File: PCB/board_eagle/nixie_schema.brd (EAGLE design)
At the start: 150 x 170 mm, 102 parts, among them P1 100k, Q1 BC856B, Q2 IRF740S, U2 MC7940N

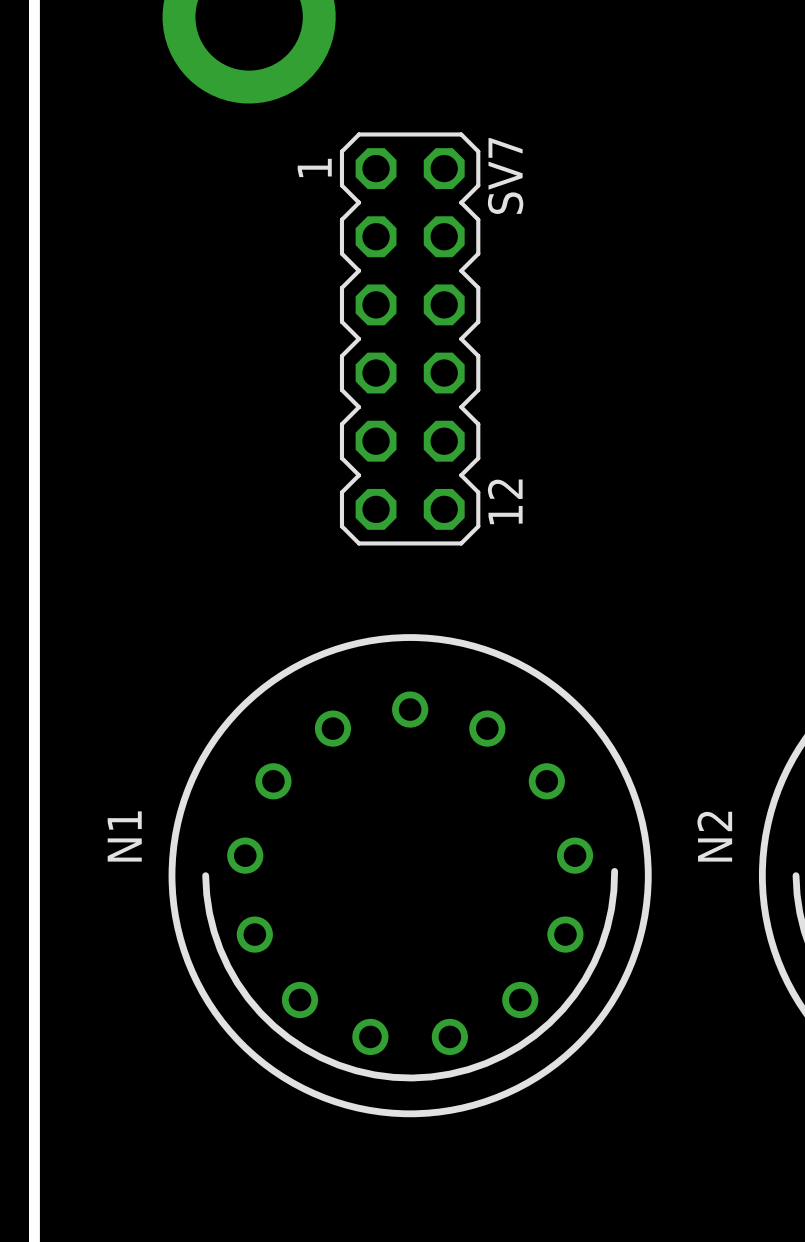
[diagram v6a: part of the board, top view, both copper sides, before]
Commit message: Top board first route
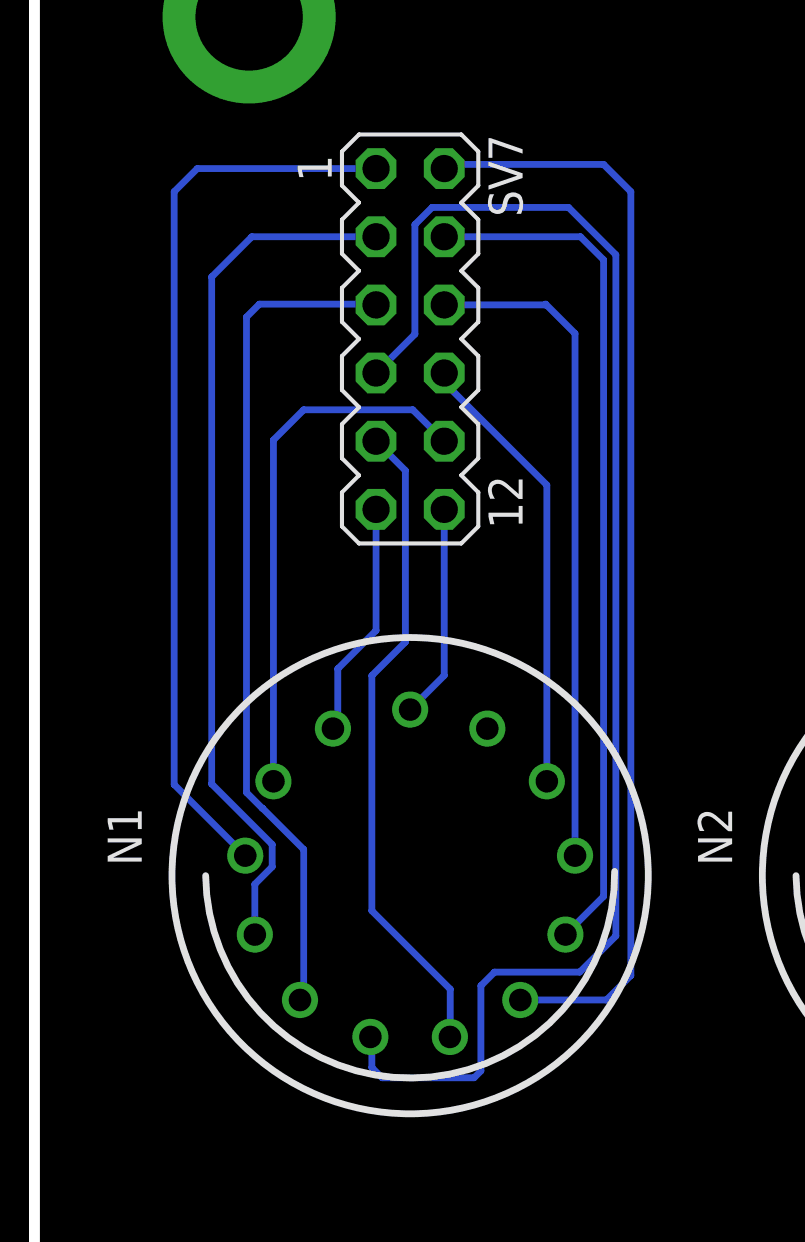
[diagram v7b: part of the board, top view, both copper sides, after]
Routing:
- net N$30: track 0.00 -> 54.5 mm
- net N$28: track 0.00 -> 41.1 mm
- net N$33: track 0.00 -> 33.7 mm
- net N$32: track 0.00 -> 32.5 mm
- net N$27: track 0.00 -> 32.0 mm
- net N$31: track 0.00 -> 31.4 mm
- net N$26: track 0.00 -> 24.8 mm
- net N$29: track 0.00 -> 24.4 mm
- net N$24: track 0.00 -> 20.0 mm
- net N$25: track 0.00 -> 16.8 mm
- net N$94: track 0.00 -> 8.83 mm
- net N$10: track 0.00 -> 7.99 mm
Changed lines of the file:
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@@
 <contactref element="SV7" pad="10"/>
 <contactref element="N1" pad="0"/>
-<wire x1="15.27" y1="-33.81" x2="8.9058" y2="-46.4837" width="0" layer="19" extent="1-1"/>
+<wire x1="8.9058" y1="-33.7662" x2="10.033" y2="-32.639" width="0.254" layer="16"/>
+<wire x1="10.033" y1="-32.639" x2="14.099" y2="-32.639" width="0.254" layer="16"/>
+<wire x1="14.099" y1="-32.639" x2="15.27" y2="-33.81" width="0.254" layer="16"/>
+<wire x1="8.9058" y1="-46.4837" x2="8.9058" y2="-33.7662" width="0.254" layer="16"/>
 </signal>
 <signal name="N$25">
 <contactref element="SV7" pad="8"/>
 <contactref element="N1" pad="1"/>
-<wire x1="15.27" y1="-31.27" x2="19.0942" y2="-46.4837" width="0" layer="19" extent="1-1"/>
+<wire x1="15.27" y1="-31.6188125" x2="15.27" y2="-31.27" width="0.254" layer="16"/>
+<wire x1="19.0942" y1="-46.4837" x2="19.0942" y2="-35.4430125" width="0.254" layer="16"/>
+<wire x1="19.0942" y1="-35.4430125" x2="15.27" y2="-31.6188125" width="0.254" layer="16"/>
 </signal>
 <signal name="N$26">
 <contactref element="SV7" pad="6"/>
 <contactref element="N1" pad="2"/>
-<wire x1="15.27" y1="-28.73" x2="20.1448" y2="-49.2539" width="0" layer="19" extent="1-1"/>
+<wire x1="20.1448" y1="-49.2539" x2="20.1448" y2="-29.7968" width="0.254" layer="16"/>
+<wire x1="19.05" y1="-28.702" x2="20.1448" y2="-29.7968" width="0.254" layer="16"/>
+<wire x1="15.27" y1="-28.73" x2="19.022" y2="-28.73" width="0.254" layer="16"/>
+<wire x1="19.022" y1="-28.73" x2="19.05" y2="-28.702" width="0.254" layer="16"/>
 </signal>
 <signal name="N$27">
 <contactref element="SV7" pad="4"/>
 <contactref element="N1" pad="3"/>
-<wire x1="15.27" y1="-26.19" x2="19.7877" y2="-52.195" width="0" layer="19" extent="1-1"/>
+<wire x1="15.27" y1="-26.19" x2="20.348" y2="-26.19" width="0.254" layer="16"/>
+<wire x1="20.348" y1="-26.19" x2="21.209" y2="-27.051" width="0.254" layer="16"/>
+<wire x1="21.209" y1="-27.051" x2="21.209" y2="-50.7737" width="0.254" layer="16"/>
+<wire x1="21.209" y1="-50.7737" x2="19.7877" y2="-52.195" width="0.254" layer="16"/>
 </signal>
 <signal name="N$28">
 <contactref element="SV7" pad="2"/>
 <contactref element="N1" pad="4"/>
-<wire x1="15.27" y1="-23.65" x2="18.1047" y2="-54.6332" width="0" layer="19" extent="1-1"/>
+<wire x1="18.1047" y1="-54.6332" x2="21.3128" y2="-54.6332" width="0.254" layer="16"/>
+<wire x1="21.3128" y1="-54.6332" x2="22.225" y2="-53.721" width="0.254" layer="16"/>
+<wire x1="22.225" y1="-53.721" x2="22.225" y2="-24.511" width="0.254" layer="16"/>
+<wire x1="22.225" y1="-24.511" x2="21.209" y2="-23.495" width="0.254" layer="16"/>
+<wire x1="21.209" y1="-23.495" x2="15.425" y2="-23.495" width="0.254" layer="16"/>
+<wire x1="15.425" y1="-23.495" x2="15.27" y2="-23.65" width="0.254" layer="16"/>
 </signal>
 <signal name="N$29">
 <contactref element="SV7" pad="9"/>
 <contactref element="N1" pad="5"/>
-<wire x1="12.73" y1="-33.81" x2="15.4813" y2="-56.0101" width="0" layer="19" extent="1-1"/>
+<wire x1="12.73" y1="-33.81" x2="13.8222" y2="-34.9022" width="0.254" layer="16"/>
+<wire x1="13.8222" y1="-41.2958" x2="12.573" y2="-42.545" width="0.254" layer="16"/>
+<wire x1="12.573" y1="-42.545" x2="12.573" y2="-51.308" width="0.254" layer="16"/>
+<wire x1="12.573" y1="-51.308" x2="15.494" y2="-54.229" width="0.254" layer="16"/>
+<wire x1="15.494" y1="-54.229" x2="15.494" y2="-55.9974" width="0.254" layer="16"/>
+<wire x1="15.494" y1="-55.9974" x2="15.4813" y2="-56.0101" width="0.254" layer="16"/>
+<wire x1="13.8222" y1="-34.9022" x2="13.8222" y2="-41.2958" width="0.254" layer="16"/>
 </signal>
 <signal name="N$30">
 <contactref element="SV7" pad="7"/>
 <contactref element="N1" pad="6"/>
-<wire x1="12.73" y1="-31.27" x2="12.5187" y2="-56.0101" width="0" layer="19" extent="1-1"/>
+<wire x1="14.81759375" y1="-25.0978" x2="14.1778" y2="-25.73759375" width="0.254" layer="16"/>
+<wire x1="19.90238125" y1="-25.0978" x2="21.6662" y2="-26.86161875" width="0.254" layer="16"/>
+<wire x1="19.90238125" y1="-25.0978" x2="14.81759375" y2="-25.0978" width="0.254" layer="16"/>
+<wire x1="14.1778" y1="-29.8222" x2="12.73" y2="-31.27" width="0.254" layer="16"/>
+<wire x1="14.1778" y1="-25.73759375" x2="14.1778" y2="-29.8222" width="0.254" layer="16"/>
+<wire x1="21.6662" y1="-52.2478" x2="20.32" y2="-53.594" width="0.254" layer="16"/>
+<wire x1="20.32" y1="-53.594" x2="17.145" y2="-53.594" width="0.254" layer="16"/>
+<wire x1="17.145" y1="-53.594" x2="16.637" y2="-54.102" width="0.254" layer="16"/>
+<wire x1="16.637" y1="-54.102" x2="16.637" y2="-57.277" width="0.254" layer="16"/>
+<wire x1="16.637" y1="-57.277" x2="16.383" y2="-57.531" width="0.254" layer="16"/>
+<wire x1="16.383" y1="-57.531" x2="12.954" y2="-57.531" width="0.254" layer="16"/>
+<wire x1="12.954" y1="-57.531" x2="12.573" y2="-57.15" width="0.254" layer="16"/>
+<wire x1="12.573" y1="-57.15" x2="12.573" y2="-56.0644" width="0.254" layer="16"/>
+<wire x1="12.573" y1="-56.0644" x2="12.5187" y2="-56.0101" width="0.254" layer="16"/>
+<wire x1="21.6662" y1="-26.86161875" x2="21.6662" y2="-52.2478" width="0.254" layer="16"/>
 </signal>
 <signal name="N$31">
 <contactref element="SV7" pad="5"/>
 <contactref element="N1" pad="7"/>
-<wire x1="12.73" y1="-28.73" x2="9.8953" y2="-54.6332" width="0" layer="19" extent="1-1"/>
+<wire x1="8.48984375" y1="-47.4879" x2="8.4989" y2="-47.4879" width="0.254" layer="16"/>
+<wire x1="8.4989" y1="-47.4879" x2="10.033" y2="-49.022" width="0.254" layer="16"/>
+<wire x1="10.033" y1="-49.022" x2="10.033" y2="-54.4955" width="0.254" layer="16"/>
+<wire x1="10.033" y1="-54.4955" x2="9.8953" y2="-54.6332" width="0.254" layer="16"/>
+<wire x1="8.48984375" y1="-47.4879" x2="7.9016" y2="-46.89965625" width="0.254" layer="16"/>
+<wire x1="7.9016" y1="-29.1824" x2="8.382" y2="-28.702" width="0.254" layer="16"/>
+<wire x1="8.382" y1="-28.702" x2="12.702" y2="-28.702" width="0.254" layer="16"/>
+<wire x1="12.702" y1="-28.702" x2="12.73" y2="-28.73" width="0.254" layer="16"/>
+<wire x1="7.9016" y1="-46.89965625" x2="7.9016" y2="-29.1824" width="0.254" layer="16"/>
 </signal>
 <signal name="N$32">
 <contactref element="SV7" pad="3"/>
 <contactref element="N1" pad="8"/>
-<wire x1="12.73" y1="-26.19" x2="8.2123" y2="-52.195" width="0" layer="19" extent="1-1"/>
+<wire x1="12.73" y1="-26.19" x2="8.1" y2="-26.19" width="0.254" layer="16"/>
+<wire x1="8.1" y1="-26.19" x2="6.604" y2="-27.686" width="0.254" layer="16"/>
+<wire x1="8.8594" y1="-48.83794375" x2="8.8594" y2="-49.66985625" width="0.254" layer="16"/>
+<wire x1="6.604" y1="-27.686" x2="6.604" y2="-46.58254375" width="0.254" layer="16"/>
+<wire x1="6.604" y1="-46.58254375" x2="8.8594" y2="-48.83794375" width="0.254" layer="16"/>
+<wire x1="8.8594" y1="-49.66985625" x2="8.2123" y2="-50.31695625" width="0.254" layer="16"/>
+<wire x1="8.2123" y1="-50.31695625" x2="8.2123" y2="-52.195" width="0.254" layer="16"/>
 </signal>
 <signal name="N$33">
 <contactref element="SV7" pad="1"/>
 <contactref element="N1" pad="9"/>
-<wire x1="12.73" y1="-23.65" x2="7.8552" y2="-49.2539" width="0" layer="19" extent="1-1"/>
+<wire x1="12.73" y1="-23.65" x2="6.068" y2="-23.65" width="0.254" layer="16"/>
+<wire x1="6.068" y1="-23.65" x2="5.207" y2="-24.511" width="0.254" layer="16"/>
+<wire x1="5.207" y1="-24.511" x2="5.207" y2="-46.6057" width="0.254" layer="16"/>
+<wire x1="5.207" y1="-46.6057" x2="7.8552" y2="-49.2539" width="0.254" layer="16"/>
 </signal>
 <signal name="N$35">
@@
 <contactref element="SV7" pad="12"/>
 <contactref element="N1" pad="A"/>
-<wire x1="15.27" y1="-36.35" x2="14" y2="-43.8101" width="0" layer="19" extent="1-1"/>
+<wire x1="15.27" y1="-36.35" x2="15.27" y2="-42.5401" width="0.254" layer="16"/>
+<wire x1="15.27" y1="-42.5401" x2="14" y2="-43.8101" width="0.254" layer="16"/>
 </signal>
 <signal name="N$19">
@@
 <wire x1="66.894" y1="16.256" x2="66.9" y2="16.25" width="0.2032" layer="1"/>
 <wire x1="58.71" y1="71.78" x2="57.7394" y2="77.2446" width="0" layer="19" extent="1-1"/>
-<wire x1="60.833" y1="16.256" x2="58.71" y2="71.78" width="0" layer="19" extent="1-1"/>
+<wire x1="61.468" y1="16.256" x2="58.71" y2="71.78" width="0" layer="19" extent="1-1"/>
 </signal>
 <signal name="N$22">
@@
 <contactref element="SV7" pad="11"/>
 <contactref element="N1" pad="LHDP"/>
-<wire x1="12.73" y1="-36.35" x2="11.1234" y2="-44.5191" width="0" layer="19" extent="1-1"/>
+<wire x1="12.73" y1="-36.35" x2="12.73" y2="-40.864" width="0.254" layer="16"/>
+<wire x1="12.73" y1="-40.864" x2="11.303" y2="-42.291" width="0.254" layer="16"/>
+<wire x1="11.303" y1="-42.291" x2="11.303" y2="-44.3395" width="0.254" layer="16"/>
+<wire x1="11.303" y1="-44.3395" x2="11.1234" y2="-44.5191" width="0.254" layer="16"/>
 </signal>
 <signal name="N$86">
